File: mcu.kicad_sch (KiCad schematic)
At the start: 24 parts, among them J2 Conn_01x05, J3 Conn_01x10, J4 Conn_01x10, Q1 MMBT3904, Q3 MMBT3904, SW1 SW_Push, SW2 SW_Push, SW3 SW_Push, U1 CH340C, U4 ESP32-S3-WROOM-1

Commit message: Use basic parts where possible
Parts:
- C15, C16, C18: footprint Capacitor_SMD:C_0603_1608Metric_Pad1.08x0.95mm_HandSolder -> Capacitor_SMD:C_0603_1608Metric
- C21: footprint Capacitor_SMD:C_0603_1608Metric_Pad1.08x0.95mm_HandSolder -> Capacitor_SMD:C_0603_1608Metric; LCSC PN C29936 -> C15849
- R10, R11, R12, R6, R9: footprint Resistor_SMD:R_0603_1608Metric_Pad0.98x0.95mm_HandSolder -> Resistor_SMD:R_0603_1608Metric; LCSC PN C98220 -> C25804
- R7, R8: footprint Resistor_SMD:R_0603_1608Metric_Pad0.98x0.95mm_HandSolder -> Resistor_SMD:R_0603_1608Metric; LCSC PN C99782 -> C23162
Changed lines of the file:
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@@
 			)
 		)
-		(property "Footprint" "Resistor_SMD:R_0603_1608Metric_Pad0.98x0.95mm_HandSolder"
+		(property "Footprint" "Resistor_SMD:R_0603_1608Metric"
 			(at 46.228 87.63 90)
 			(effects
@@
 			)
 		)
-		(property "LCSC PN" "C99782"
+		(property "LCSC PN" "C23162"
 			(at 44.45 87.63 0)
 			(effects
@@
 			)
 		)
-		(property "Footprint" "Resistor_SMD:R_0603_1608Metric_Pad0.98x0.95mm_HandSolder"
+		(property "Footprint" "Resistor_SMD:R_0603_1608Metric"
 			(at 104.902 124.46 90)
 			(effects
@@
 			)
 		)
-		(property "LCSC PN" "C98220"
+		(property "LCSC PN" "C25804"
 			(at 106.68 124.46 0)
 			(effects
@@
 			)
 		)
-		(property "Footprint" "Resistor_SMD:R_0603_1608Metric_Pad0.98x0.95mm_HandSolder"
+		(property "Footprint" "Resistor_SMD:R_0603_1608Metric"
 			(at 41.402 124.46 90)
 			(effects
@@
 			)
 		)
-		(property "LCSC PN" "C98220"
+		(property "LCSC PN" "C25804"
 			(at 43.18 124.46 0)
 			(effects
@@
 			)
 		)
-		(property "Footprint" "Capacitor_SMD:C_0603_1608Metric_Pad1.08x0.95mm_HandSolder"
+		(property "Footprint" "Capacitor_SMD:C_0603_1608Metric"
 			(at 84.7852 139.7 0)
 			(effects
@@
 			)
 		)
-		(property "LCSC PN" "C29936"
+		(property "LCSC PN" "C15849"
 			(at 83.82 135.89 0)
 			(effects
@@
 			)
 		)
-		(property "Footprint" "Resistor_SMD:R_0603_1608Metric_Pad0.98x0.95mm_HandSolder"
+		(property "Footprint" "Resistor_SMD:R_0603_1608Metric"
 			(at 248.92 64.008 90)
 			(effects
@@
 			)
 		)
-		(property "LCSC PN" "C98220"
+		(property "LCSC PN" "C25804"
 			(at 248.92 62.23 90)
 			(effects
@@
 			)
 		)
-		(property "Footprint" "Resistor_SMD:R_0603_1608Metric_Pad0.98x0.95mm_HandSolder"
+		(property "Footprint" "Resistor_SMD:R_0603_1608Metric"
 			(at 69.342 124.46 90)
 			(effects
@@
 			)
 		)
-		(property "LCSC PN" "C98220"
+		(property "LCSC PN" "C25804"
 			(at 71.12 124.46 0)
 			(effects
@@
 			)
 		)
-		(property "Footprint" "Capacitor_SMD:C_0603_1608Metric_Pad1.08x0.95mm_HandSolder"
+		(property "Footprint" "Capacitor_SMD:C_0603_1608Metric"
 			(at 56.1848 52.07 0)
 			(effects
@@
 			)
 		)
-		(property "Footprint" "Resistor_SMD:R_0603_1608Metric_Pad0.98x0.95mm_HandSolder"
+		(property "Footprint" "Resistor_SMD:R_0603_1608Metric"
 			(at 248.92 48.768 90)
 			(effects
@@
 			)
 		)
-		(property "LCSC PN" "C98220"
+		(property "LCSC PN" "C25804"
 			(at 248.92 46.99 90)
 			(effects
@@
 			)
 		)
-		(property "Footprint" "Capacitor_SMD:C_0603_1608Metric_Pad1.08x0.95mm_HandSolder"
+		(property "Footprint" "Capacitor_SMD:C_0603_1608Metric"
 			(at 159.0548 52.07 0)
 			(effects
@@
 			)
 		)
-		(property "Footprint" "Capacitor_SMD:C_0603_1608Metric_Pad1.08x0.95mm_HandSolder"
+		(property "Footprint" "Capacitor_SMD:C_0603_1608Metric"
 			(at 43.4848 52.07 0)
 			(effects
@@
 			)
 		)
-		(property "Footprint" "Resistor_SMD:R_0603_1608Metric_Pad0.98x0.95mm_HandSolder"
+		(property "Footprint" "Resistor_SMD:R_0603_1608Metric"
 			(at 55.118 87.63 90)
 			(effects
@@
 			)
 		)
-		(property "LCSC PN" "C99782"
+		(property "LCSC PN" "C23162"
 			(at 53.34 87.63 0)
 			(effects

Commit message: Sketch out component placement
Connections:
- net INT renamed INT1

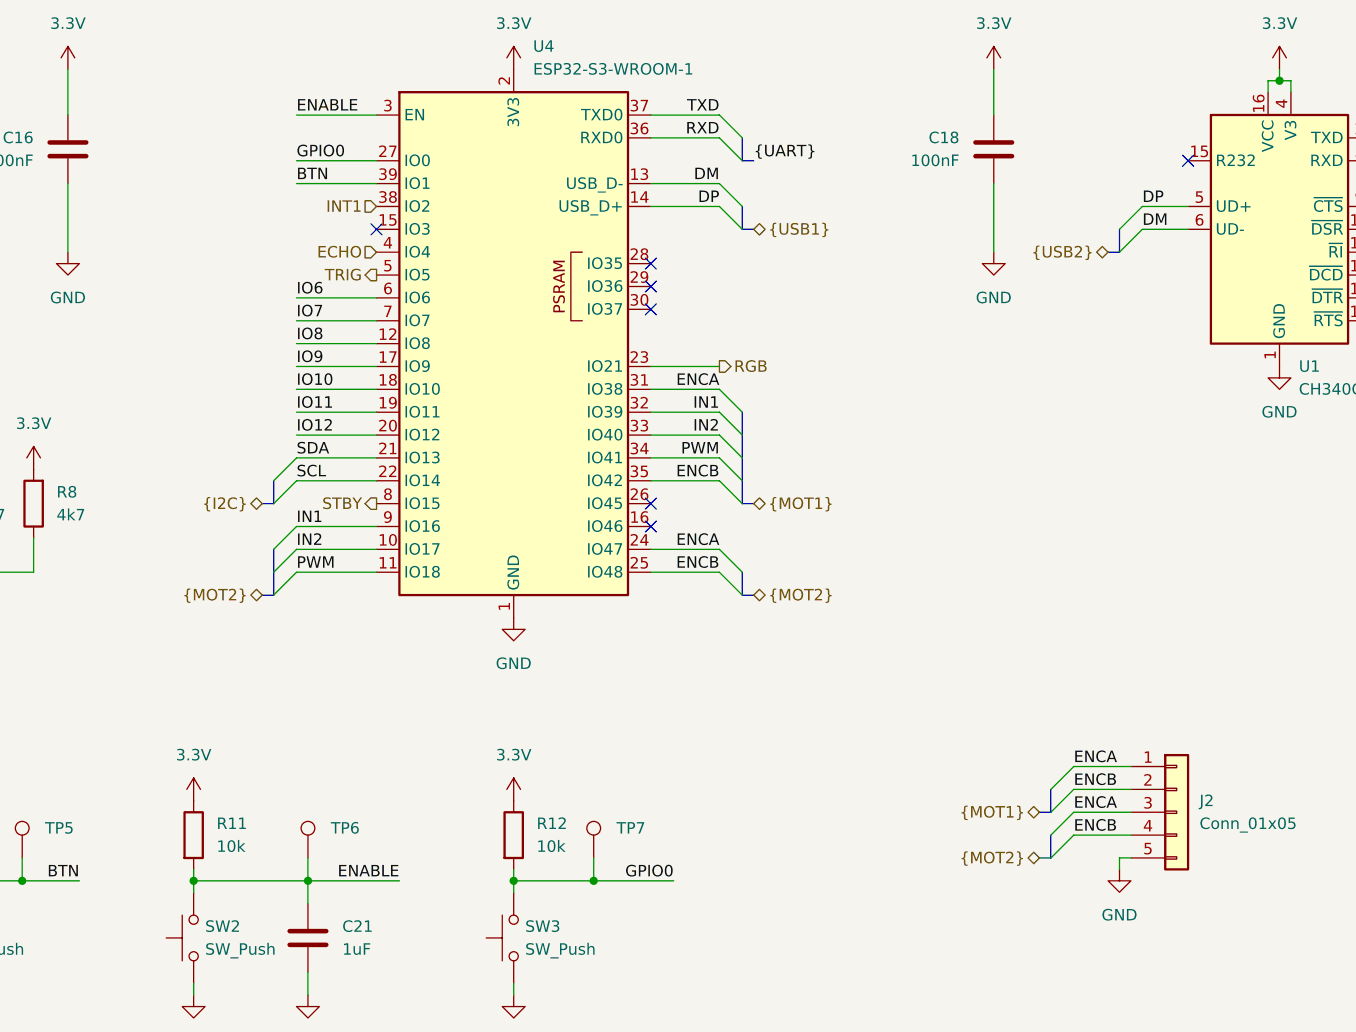
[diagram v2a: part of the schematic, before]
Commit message: Fix bus merging and add net classes
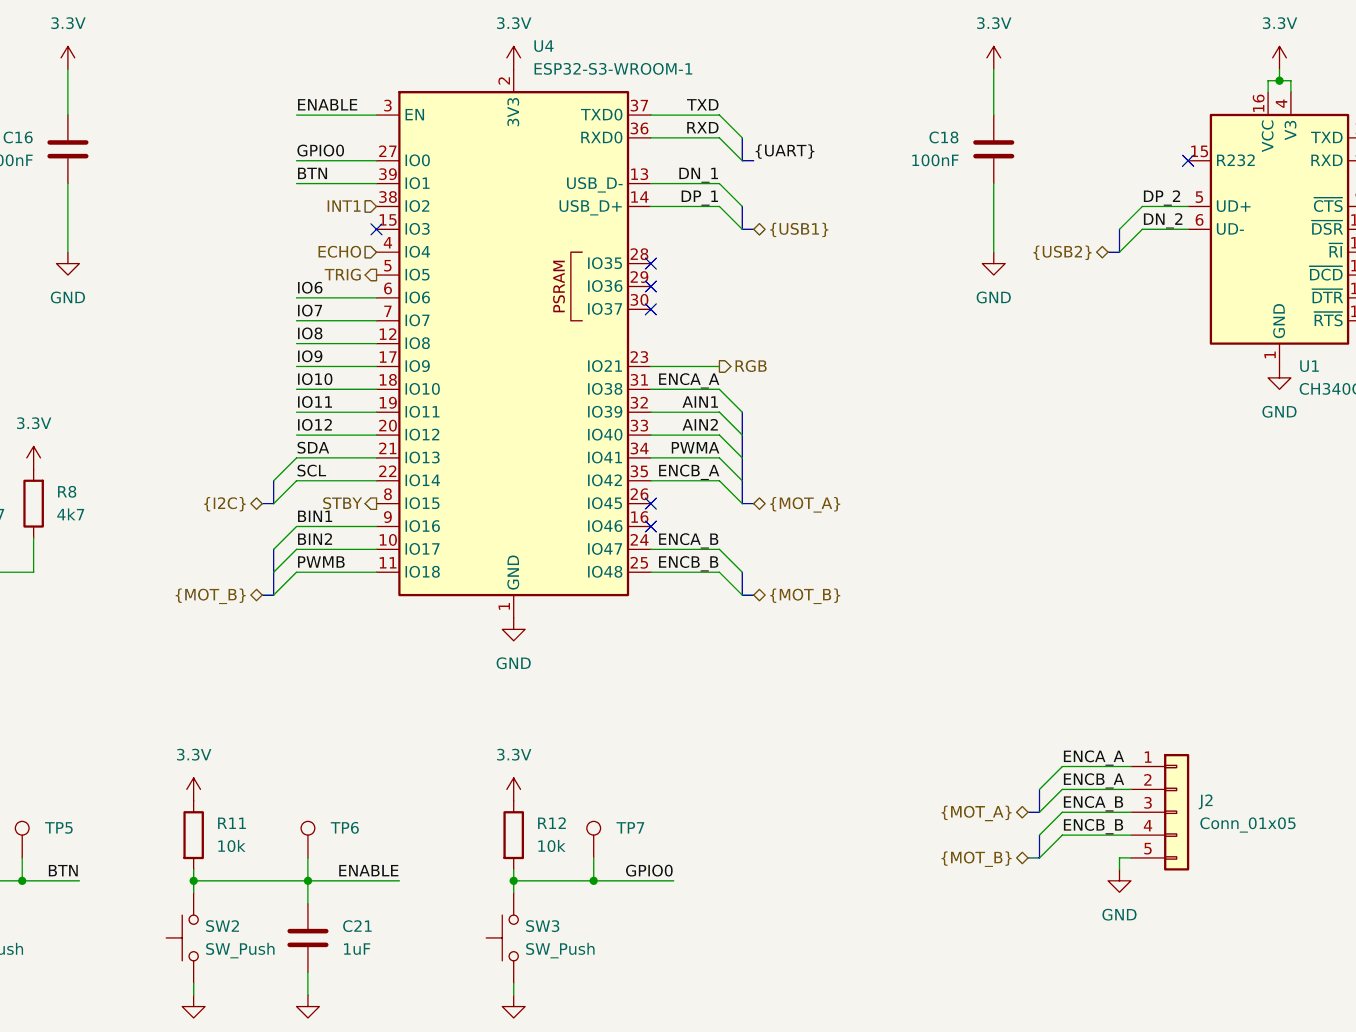
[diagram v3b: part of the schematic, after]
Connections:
- net DM renamed DN_1
- net DN_1: no longer U1.6 (UD-)
- net DP renamed DP_1
- net DP_1: no longer U1.5 (UD+)
- net ENCA renamed ENCA_A
- net ENCA_A: no longer J2.3 (Pin_3), U4.24 (IO47)
- net ENCB renamed ENCB_A
- net ENCB_A: no longer J2.4 (Pin_4), U4.25 (IO48)
- net IN1 renamed AIN1
- net AIN1: no longer U4.9 (IO16)
- net IN2 renamed AIN2
- net AIN2: no longer U4.10 (IO17)
- net PWM renamed PWMA
- net PWMA: no longer U4.11 (IO18)
- new net BIN1: U4.9 (IO16)
- new net BIN2: U4.10 (IO17)
- new net DN_2: U1.6 (UD-)
- new net DP_2: U1.5 (UD+)
- new net ENCA_B: J2.3 (Pin_3), U4.24 (IO47)
- new net ENCB_B: J2.4 (Pin_4), U4.25 (IO48)
- new net PWMB: U4.11 (IO18)

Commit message: Start conceptual layouting
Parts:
- removed TP5, TP6, TP7: TestPoint, TestPoint:TestPoint_Pad_D1.5mm, symbol Connector:TestPoint
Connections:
- net IO8: now also U4.23 (IO21); no longer U4.12 (IO8)
- net RGB: now also U4.12 (IO8); no longer U4.23 (IO21)

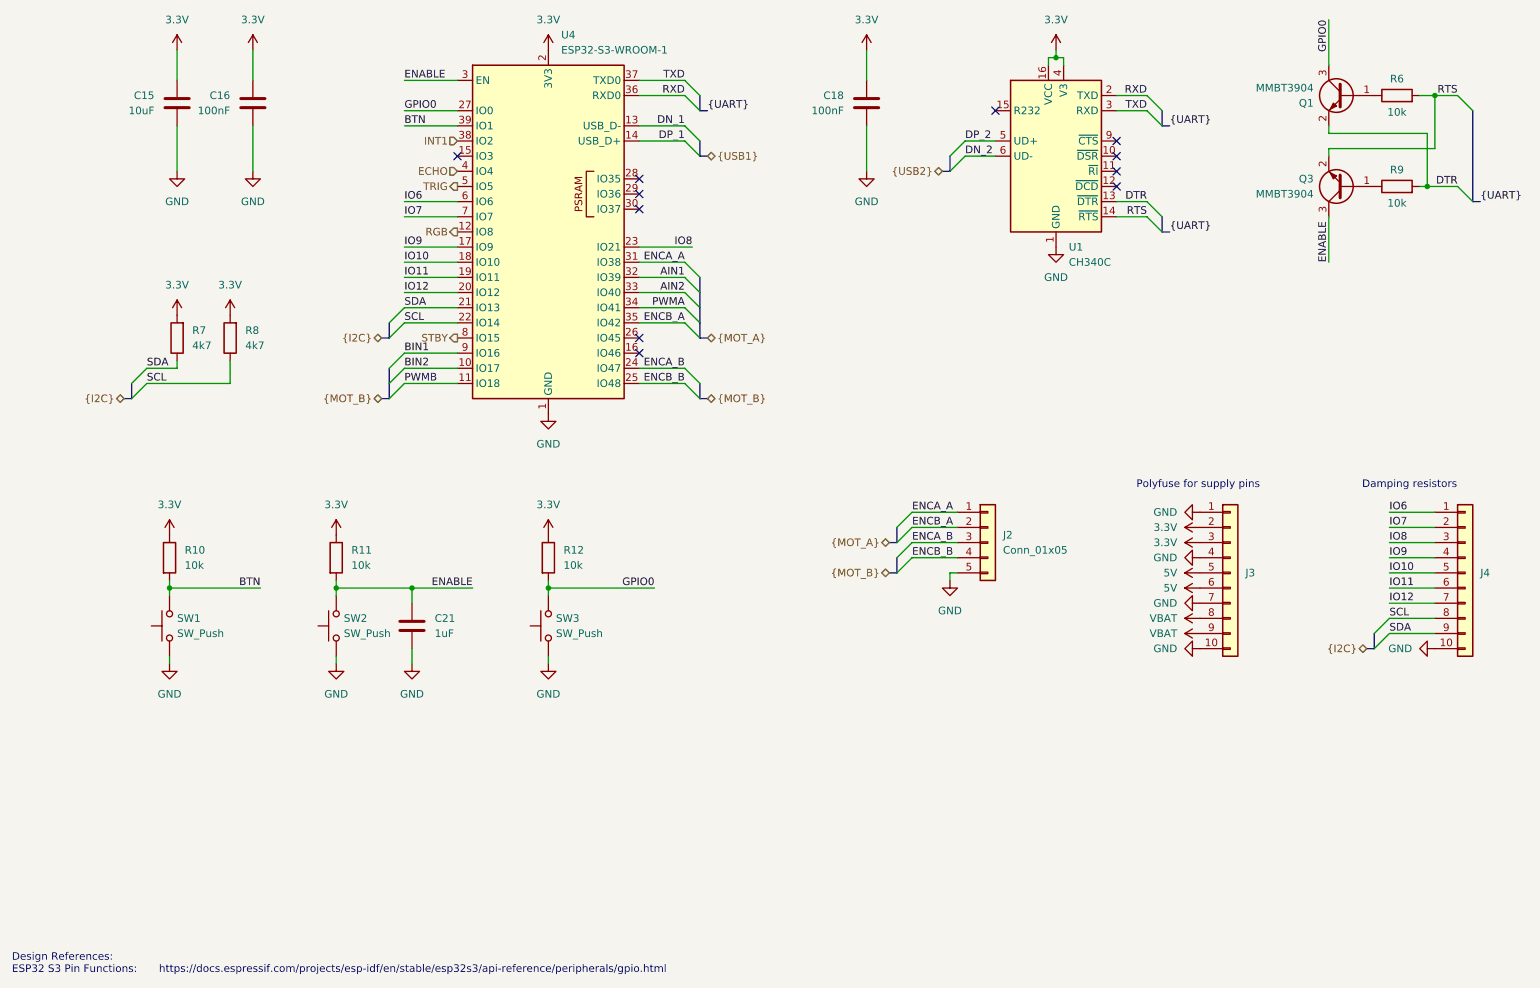
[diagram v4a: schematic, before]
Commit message: Continue layout and update schematic
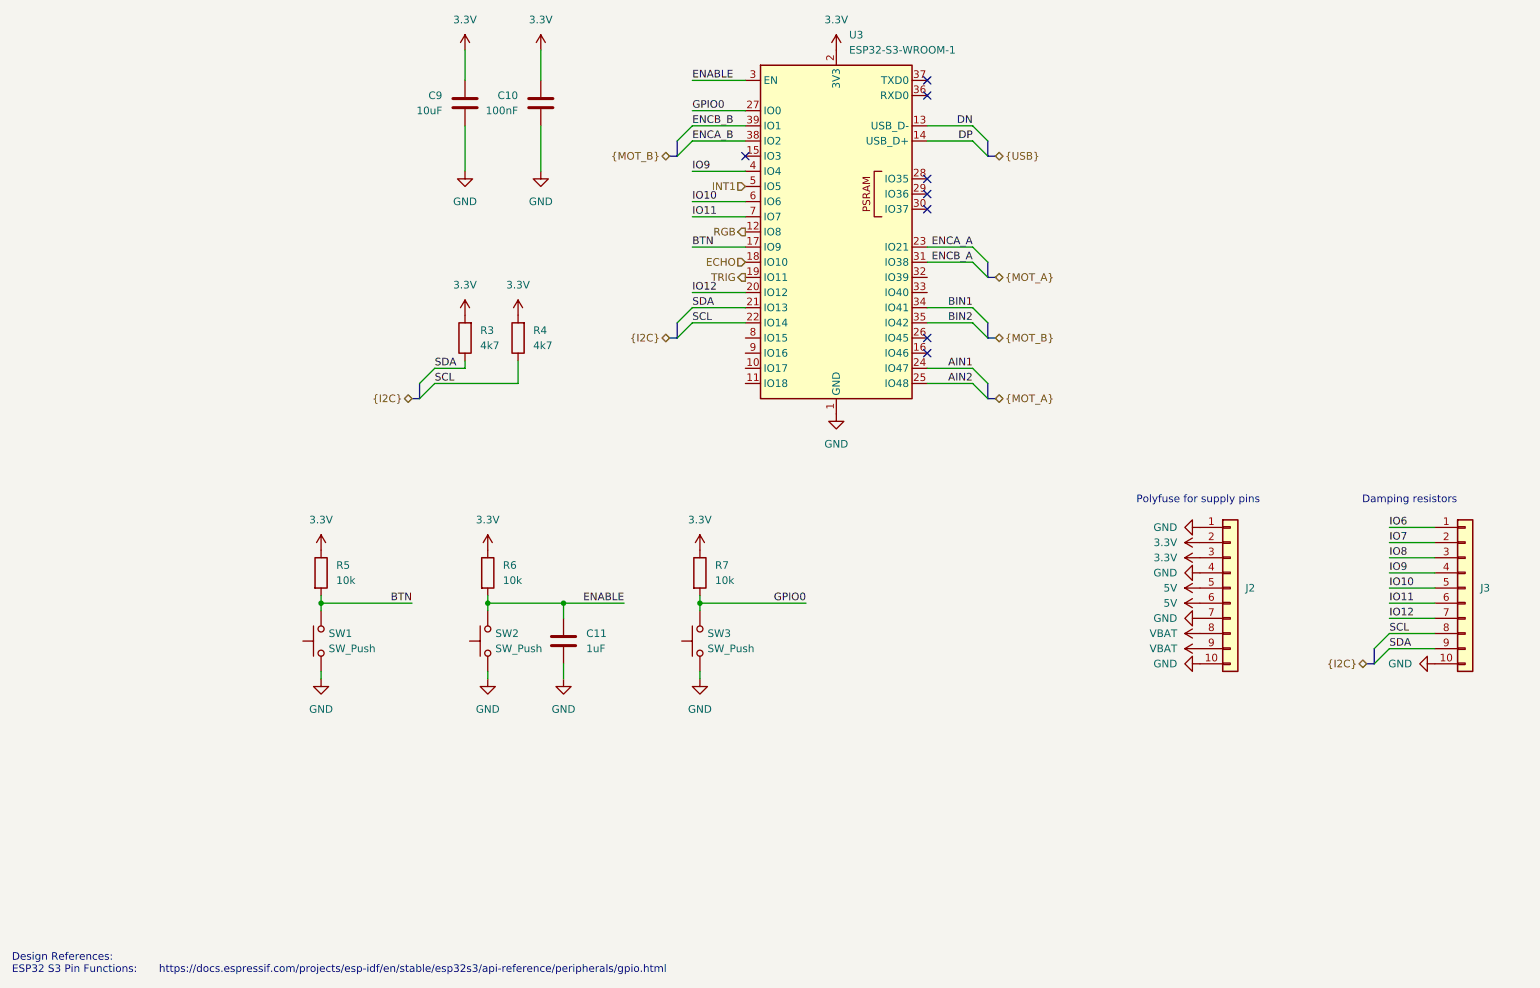
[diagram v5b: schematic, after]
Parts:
- removed C18: 100nF, Capacitor_SMD:C_0603_1608Metric, symbol Device:C
- removed J2: Conn_01x05, Connector_PinHeader_2.54mm:PinHeader_1x05_P2.54mm_Vertical, symbol Connector_Generic:Conn_01x05
- removed Q1, Q3: MMBT3904, Package_TO_SOT_SMD:SOT-23, symbol Transistor_BJT:MMBT3904
- removed R6, R9: 10k, Resistor_SMD:R_0603_1608Metric, symbol Device:R
- removed U1: CH340C, Package_SO:SOIC-16_3.9x9.9mm_P1.27mm, symbol Interface_USB:CH340C
- renumbered C16 to C10, C21 to C11, C15 to C9, J3 to J2, J4 to J3, R7 to R3, R8 to R4, R10 to R5, R11 to R6, R12 to R7, U4 to U3
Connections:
- net PWMA is gone; now on net BIN1: U3.34 (IO41)
- net AIN1: now also U3.24 (IO47); no longer U3.32 (IO39)
- net AIN2: now also U3.25 (IO48); no longer U3.33 (IO40)
- net BIN1: no longer U3.9 (IO16)
- net BIN2: now also U3.35 (IO42); no longer U3.10 (IO17)
- net BTN: now also U3.17 (IO9); no longer U3.39 (IO1)
- net ECHO: now also U3.18 (IO10); no longer U3.4 (IO4)
- net ENCA_A: now also U3.23 (IO21); no longer U3.31 (IO38)
- net ENCA_B: now also U3.38 (IO2); no longer U3.24 (IO47)
- net ENCB_A: now also U3.31 (IO38); no longer U3.35 (IO42)
- net ENCB_B: now also U3.39 (IO1); no longer U3.25 (IO48)
- net INT1: now also U3.5 (IO5); no longer U3.38 (IO2)
- net IO10: now also U3.6 (IO6); no longer U3.18 (IO10)
- net IO11: now also U3.7 (IO7); no longer U3.19 (IO11)
- net IO6: no longer U3.6 (IO6)
- net IO7: no longer U3.7 (IO7)
- net IO8: no longer U3.23 (IO21)
- net IO9: now also U3.4 (IO4); no longer U3.17 (IO9)
- net TRIG: now also U3.19 (IO11); no longer U3.5 (IO5)
- net DN_1 renamed DN
- net DP_1 renamed DP
- net PWMB: no longer names the net of U3.11 (IO18)
- net RXD: no longer names the net of U3.36 (RXD0)
- net STBY: no longer names the net of U3.8 (IO15)
- net TXD: no longer names the net of U3.37 (TXD0)
- no-connect marks 11 -> 8
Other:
- moved on the sheet: C10, C11, C9, J2, J3, R3, R4, R5, R6, R7, SW1, SW2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
